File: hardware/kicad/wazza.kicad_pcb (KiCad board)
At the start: 2 copper layers, 155 x 26 mm, 24 parts, among them J1 USB_C_Receptacle_GCT_USB4105-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, J2 PinHeader_1x03_P2.54mm_Vertic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, SW2 SW_SPST_B3S-1000, SW3 SW_SPST_B3S-1000, U1 SOT-23-5, U12 QFN-16-1EP_3x3mm_P0.5mm_EP1.7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, U13 LGA-24L_3x3.5mm_P0.43mm, U14 PinHeader_1x04_P2.54mm_Vertic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, U2 SOT-23-5, U9 ESP32-S3-WROOM-1

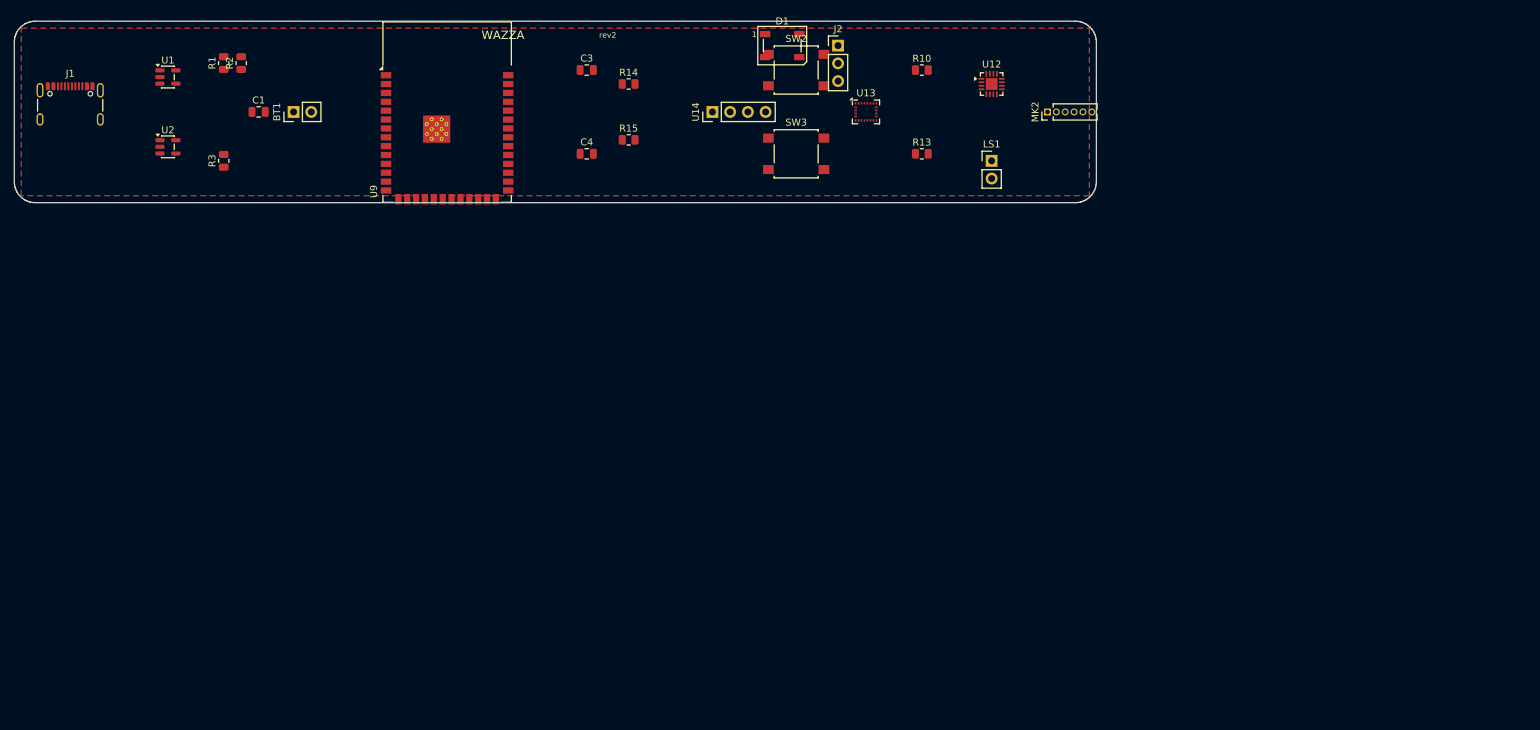
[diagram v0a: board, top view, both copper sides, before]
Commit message: Update routed KiCad PCB, Gerbers, STEP, and assembly/wiring docs.
Refreshes fab outputs from the autorouted board and documents build/fit notes for resubmission.

Co-authored-by: Cursor <cursoragent@cursor.com>
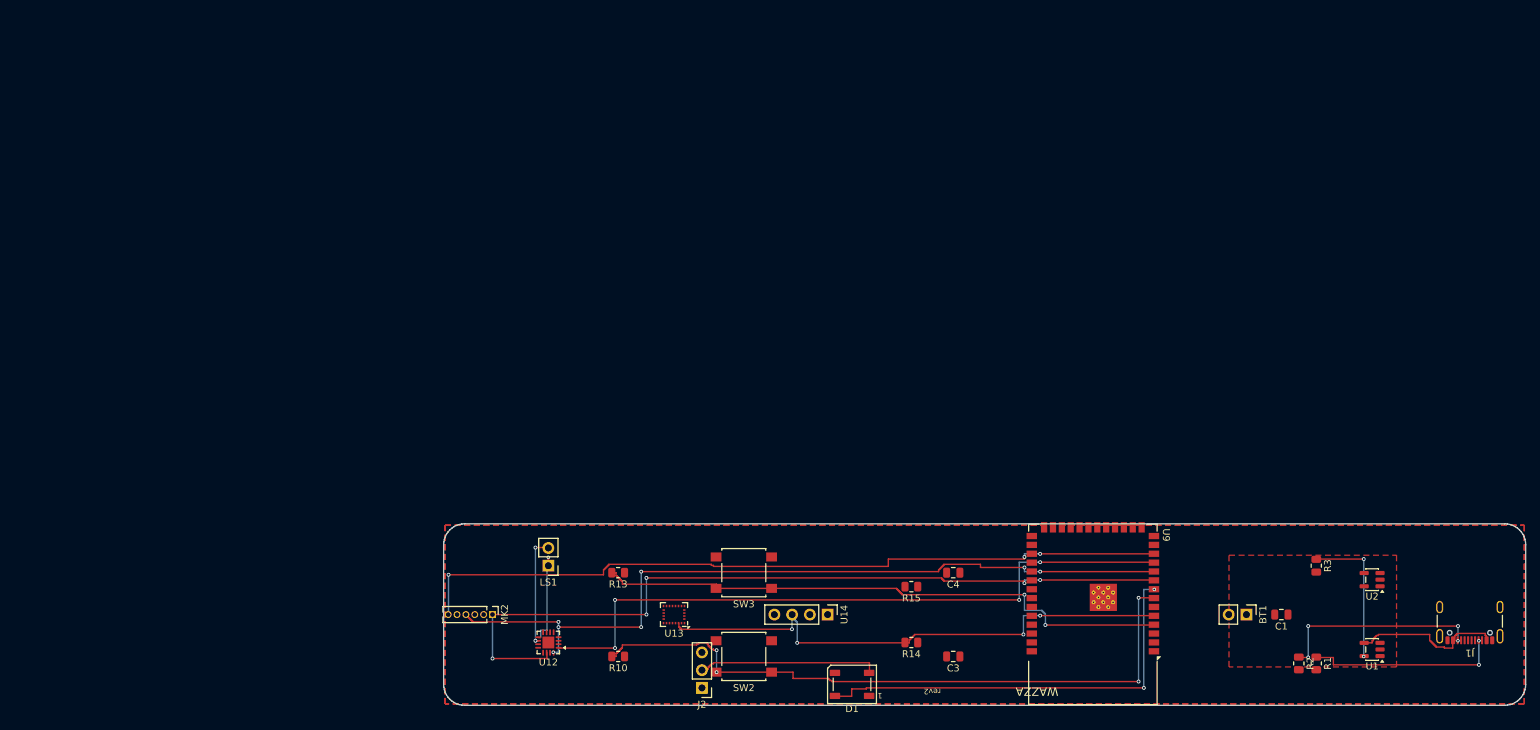
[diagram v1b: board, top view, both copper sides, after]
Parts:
- moved J1 213.0 mm to (208.5, 85.0), turned to 180 degrees
- moved U1 191.0 mm to (194.5, 90.0), turned to 180 degrees
- moved U2 183.3 mm to (194.5, 80.0), turned to 180 degrees
- moved R1 178.6 mm to (186.5, 92.0), turned to -90 degrees
- moved R2 174.2 mm to (184.0, 92.0), turned to -90 degrees
- moved R3 166.9 mm to (186.5, 78.0), turned to -90 degrees
- moved C1 163.2 mm to (181.5, 85.0), turned to 180 degrees
- moved BT1 154.3 mm to (176.5, 85.0), turned to -90 degrees
- moved U9 117.2 mm to (154.5, 85.0), turned to 180 degrees
- moved MK2 107.3 mm to (68.5, 85.0), turned to -90 degrees
- moved U12 102.1 mm to (76.5, 89.0), turned to 180 degrees
- moved C3 99.1 mm to (134.5, 91.0), turned to 180 degrees
- moved R10 94.6 mm to (86.5, 91.0), turned to 180 degrees
- moved J2 94.0 mm to (98.5, 95.5), turned to 180 degrees
- moved D1 92.0 mm to (120.0, 95.0), turned to 180 degrees
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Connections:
- BT1 pad 1: (no net) -> Net-(BT1-+)
- BT1 pad 2: (no net) -> GND
- C1 pad 1: (no net) -> +3V3
- C1 pad 2: (no net) -> GND
- C3 pad 1: (no net) -> +3V3
- C3 pad 2: (no net) -> GND
- C4 pad 1: (no net) -> +3V3
- C4 pad 2: (no net) -> GND
- D1 pad 1: (no net) -> +3V3
- D1 pad 2: (no net) -> /05_LEDs_Buttons/LED_DOUT
- D1 pad 3: (no net) -> GND
- D1 pad 4: (no net) -> LED_DIN
- J1 pad A1: (no net) -> GND
- J1 pad A12: (no net) -> GND
- J1 pad A4: (no net) -> Net-(U1-VDD)
- J1 pad A5: (no net) -> Net-(J1-CC1)
- J1 pad A6: (no net) -> unconnected-(J1-D+-PadA6)
- J1 pad A7: (no net) -> unconnected-(J1-D--PadA7)
- J1 pad A8: (no net) -> unconnected-(J1-SBU1-PadA8)
- J1 pad A9: (no net) -> Net-(U1-VDD)
- J1 pad B1: (no net) -> GND
- J1 pad B12: (no net) -> GND
- J1 pad B4: (no net) -> Net-(U1-VDD)
- J1 pad B5: (no net) -> Net-(J1-CC2)
- J1 pad B6: (no net) -> unconnected-(J1-D+-PadB6)
- J1 pad B7: (no net) -> unconnected-(J1-D--PadB7)
- J1 pad B8: (no net) -> unconnected-(J1-SBU2-PadB8)
- J1 pad B9: (no net) -> Net-(U1-VDD)
- J1 pad SH: (no net) -> GND
- J2 pad 1: (no net) -> +3V3
- J2 pad 2: (no net) -> /05_LEDs_Buttons/LED_DOUT
- J2 pad 3: (no net) -> GND
- LS1 pad 1: (no net) -> Net-(U12-OUTP)
- LS1 pad 2: (no net) -> Net-(U12-OUTN)
- MK2 pad 1: (no net) -> I2S_LRCLK
- MK2 pad 2: (no net) -> GND
- MK2 pad 3: (no net) -> GND
- MK2 pad 4: (no net) -> I2S_BCLK
- MK2 pad 5: (no net) -> +3V3
- MK2 pad 6: (no net) -> MIC_DOUT
- R1 pad 1: (no net) -> Net-(J1-CC1)
- R1 pad 2: (no net) -> GND
- R10 pad 1: (no net) -> +3V3
- R10 pad 2: (no net) -> BTN_ACTION
- R13 pad 1: (no net) -> +3V3
- R13 pad 2: (no net) -> BTN_BOOT
- R14 pad 1: (no net) -> +3V3
- R14 pad 2: (no net) -> SCL
- R15 pad 1: (no net) -> +3V3
- R15 pad 2: (no net) -> SDA
- R2 pad 1: (no net) -> Net-(J1-CC2)
- R2 pad 2: (no net) -> GND
- R3 pad 1: (no net) -> Net-(U1-PROG)
- R3 pad 2: (no net) -> GND
- SW2 pad 1: (no net) -> BTN_ACTION
- SW2 pad 2: (no net) -> GND
- SW3 pad 1: (no net) -> BTN_BOOT
- SW3 pad 2: (no net) -> GND
- U1 pad 1: (no net) -> unconnected-(U1-STAT-Pad1)
- U1 pad 2: (no net) -> GND
- U1 pad 3: (no net) -> Net-(BT1-+)
- U1 pad 4: (no net) -> Net-(U1-VDD)
- U1 pad 5: (no net) -> Net-(U1-PROG)
- U12 pad 1: (no net) -> AMP_DIN
- U12 pad 10: (no net) -> Net-(U12-OUTN)
- U12 pad 14: (no net) -> I2S_LRCLK
- U12 pad 16: (no net) -> I2S_BCLK
- U12 pad 17: (no net) -> GND
- U12 pad 2: (no net) -> unconnected-(U12-GAIN_SLOT-Pad2)
- U12 pad 4: (no net) -> unconnected-(U12-SD_MODE-Pad4)
- U12 pad 7: (no net) -> +3V3
- U12 pad 8: (no net) -> GND
- U12 pad 9: (no net) -> Net-(U12-OUTP)
- U13 pad 12: (no net) -> unconnected-(U13-INT-Pad12)
- U13 pad 13: (no net) -> +3V3
- U13 pad 18: (no net) -> GND
- U13 pad 23: (no net) -> SCL
- U13 pad 24: (no net) -> SDA
- U13 pad 8: (no net) -> +3V3
- U13 pad 9: (no net) -> GND
- U14 pad 1: (no net) -> GND
- U14 pad 2: (no net) -> +3V3
- U14 pad 3: (no net) -> SCL
- U14 pad 4: (no net) -> SDA
- U2 pad 1: (no net) -> Net-(BT1-+)
- U2 pad 2: (no net) -> GND
- U2 pad 3: (no net) -> Net-(BT1-+)
- U2 pad 4: (no net) -> unconnected-(U2-NC-Pad4)
- U2 pad 5: (no net) -> +3V3
- U9 pad 1: (no net) -> GND
- U9 pad 10: (no net) -> I2S_BCLK
- U9 pad 11: (no net) -> AMP_DIN
- U9 pad 12: (no net) -> MIC_DOUT
- U9 pad 13: (no net) -> unconnected-(U9-TXD0-Pad13)
- U9 pad 14: (no net) -> unconnected-(U9-RXD0-Pad14)
- U9 pad 2: (no net) -> +3V3
- U9 pad 3: (no net) -> +3V3
- U9 pad 4: (no net) -> BTN_BOOT
- U9 pad 5: (no net) -> SCL
- U9 pad 6: (no net) -> SDA
- U9 pad 7: (no net) -> BTN_ACTION
- U9 pad 8: (no net) -> LED_DIN
- U9 pad 9: (no net) -> I2S_LRCLK
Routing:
- net I2S_LRCLK: track 0.00 -> 116.2 mm, vias 0 -> 5
- net I2S_BCLK: track 0.00 -> 114.8 mm, vias 0 -> 7
- net MIC_DOUT: track 0.00 -> 110.4 mm, vias 0 -> 3
- net AMP_DIN: track 0.00 -> 97.7 mm, vias 0 -> 4
- net BTN_ACTION: track 0.00 -> 97.2 mm, vias 0 -> 4
- net BTN_BOOT: track 0.00 -> 85.2 mm, vias 0 -> 2
- net SCL: track 0.00 -> 78.3 mm, vias 0 -> 4
- net LED_DIN: track 0.00 -> 61.1 mm, vias 0 -> 2
- net Net-(J1-CC2): track 0.00 -> 29.4 mm, vias 0 -> 4
- net Net-(J1-CC1): track 0.00 -> 27.8 mm, vias 0 -> 2
- net /05_LEDs_Buttons/LED_DOUT: track 0.00 -> 26.5 mm
- net Net-(U1-VDD): track 0.00 -> 23.8 mm
- net Net-(U1-PROG): track 0.00 -> 20.7 mm, vias 0 -> 2
- net Net-(U12-OUTN): track 0.00 -> 15.6 mm, vias 0 -> 2
- net Net-(U12-OUTP): track 0.00 -> 14.1 mm, vias 0 -> 1
- added copper zone on F.Cu, net +3V3
- added copper zone on B.Cu, net GND
- added copper zone on F.Cu, net GND
- added copper zone on F.Cu, net Net-(BT1-+)
- removed copper zone on F.Cu, net (none)
